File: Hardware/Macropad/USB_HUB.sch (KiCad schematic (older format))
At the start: 25 parts, among them J4 USB_C_Receptacle_USB2.0, J5 USB_C_Receptacle_USB2.0, J6 USB_C_Receptacle_USB2.0, U3 TPS2044D, U4 TUSB2046b, U6 SRV05-4, U7 SRV05-4, U8 SRV05-4, X2 625L3C006M00000

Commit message: First pass of the layout done
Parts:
- removed R12: OPT, resistor_smd:R_0603_1608Metric, symbol Device:R
- removed R30: 4K7, resistor_smd:R_0603_1608Metric, symbol Device:R
- removed U3: TPS2044D, Package_SO:SOIC-16_3.9x9.9mm_P1.27mm, symbol Power_Management:TPS2044D
- added C44, C45, C46: 1uF, Capacitor_smd:C_0603_1608Metric, symbol Device:C
- added R1: 4K7, resistor_smd:R_0603_1608Metric, symbol Device:R
- C37, C39: value 100uF -> 1uF; footprint Capacitor_smd:C_1210_3225Metric -> Capacitor_smd:C_0603_1608Metric
- C38: value 100uF -> 100nF; footprint Capacitor_smd:C_1210_3225Metric -> Capacitor_smd:C_0603_1608Metric
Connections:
- net DM1_N is gone; now on net USB_D1-: R23.1
- net VBUS3 is gone; now on net +5V: C39.1, J6.A4 (VBUS), J6.A9 (VBUS), J6.B4 (VBUS), J6.B9 (VBUS), U8.5 (VP)
- net nOVRCUR1 is gone; now on net +3V3: U4.10 (OVRCUR1)
- net nOVRCUR2 is gone; now on net +3V3: U4.14 (OVRCUR2)
- net nOVRCUR3 is gone; now on net +3V3: U4.18 (OVRCUR3)
- net nOVRCUR4 is gone; now on net +3V3: U4.22 (OVRCUR4)
- net +3V3: now also C37.1, C38.1, X2.1 (EN), R1.2
- net +5V: now also J4.A4 (VBUS), J4.A9 (VBUS), J4.B4 (VBUS), J4.B9 (VBUS), J5.A4 (VBUS), J5.A9 (VBUS), J5.B4 (VBUS), J5.B9 (VBUS), U6.5 (VP), U7.5 (VP), C45.1, C46.1
- net GND: now also C44.1, C45.2, C46.2
- net USB_D2-: now reaches U7.4 (IO3)
- net USB_D2-: now also J5.A7 (D-), J5.B7 (D-), R25.1
- net USB_D3-: now reaches U8.4 (IO3)
- net USB_D3-: now also J6.A7 (D-), J6.B7 (D-), R27.1
- net at U4.4 (RESET): now also C44.2, R1.1
- net USB_D1-: now reaches U6.4 (IO3)
- net USB_D1-: now also J4.A7 (D-), J4.B7 (D-)
- net DM1n renamed D1-
- net D1-: no longer R25.2, U4.15 (DM2)
- removed net DM2_N: J4.A7 (D-), J4.B7 (D-), R25.1, U6.3 (IO2)
- removed net DM3_N: J5.A7 (D-), J5.B7 (D-), R27.1, U7.3 (IO2)
- net DM3n renamed D3-
- removed net DM4_N: J6.A7 (D-), J6.B7 (D-), R29.1, U8.3 (IO2)
- net DM4n renamed D4-
- net DP1_P renamed USB_D1+
- net USB_D1+: now also J4.A6 (D+), J4.B6 (D+), U6.3 (IO2)
- net DP1p renamed D1+
- removed net DP2_P: J4.A6 (D+), J4.B6 (D+), R24.1, U6.1 (IO1)
- net DP2p renamed D2+
- net DP3_P renamed USB_D2+
- net USB_D2+: now also R24.1, U7.3 (IO2); no longer R26.1, U7.1 (IO1)
- net DP3n renamed D3+
- net DP4_P renamed USB_D3+
- net USB_D3+: now also R26.1, U8.3 (IO2); no longer R28.1, U8.1 (IO1)
- net DP4p renamed D4+
- net USBD_N renamed USB_D0-
- net USBD_P renamed USB_D0+
- removed net VBUS1: C37.1, J4.A4 (VBUS), J4.A9 (VBUS), J4.B4 (VBUS), J4.B9 (VBUS), U6.5 (VP)
- removed net VBUS2: C38.1, J5.A4 (VBUS), J5.A9 (VBUS), J5.B4 (VBUS), J5.B9 (VBUS), U7.5 (VP)
- net nPWRON1: no longer names the net of U4.9 (PWRON1)
- net nPWRON2: no longer names the net of U4.13 (PWRON2)
- net nPWRON3: no longer names the net of U4.17 (PWRON3)
- net nPWRON4: no longer names the net of U4.21 (PWRON4)
- new net D2-: R25.2, U4.15 (DM2)
- new net USB_D4+: R28.1
- new net USB_D4-: R29.1
- no-connect marks 9 -> 19
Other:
- note added: "RC rise time 6.5ms aprox"
- note removed: "Downstream power switching"
- note removed: "TODO: \nRC POR circuit\nChoose a 6MHz crystal"
- moved on the sheet: U6, U7, U8

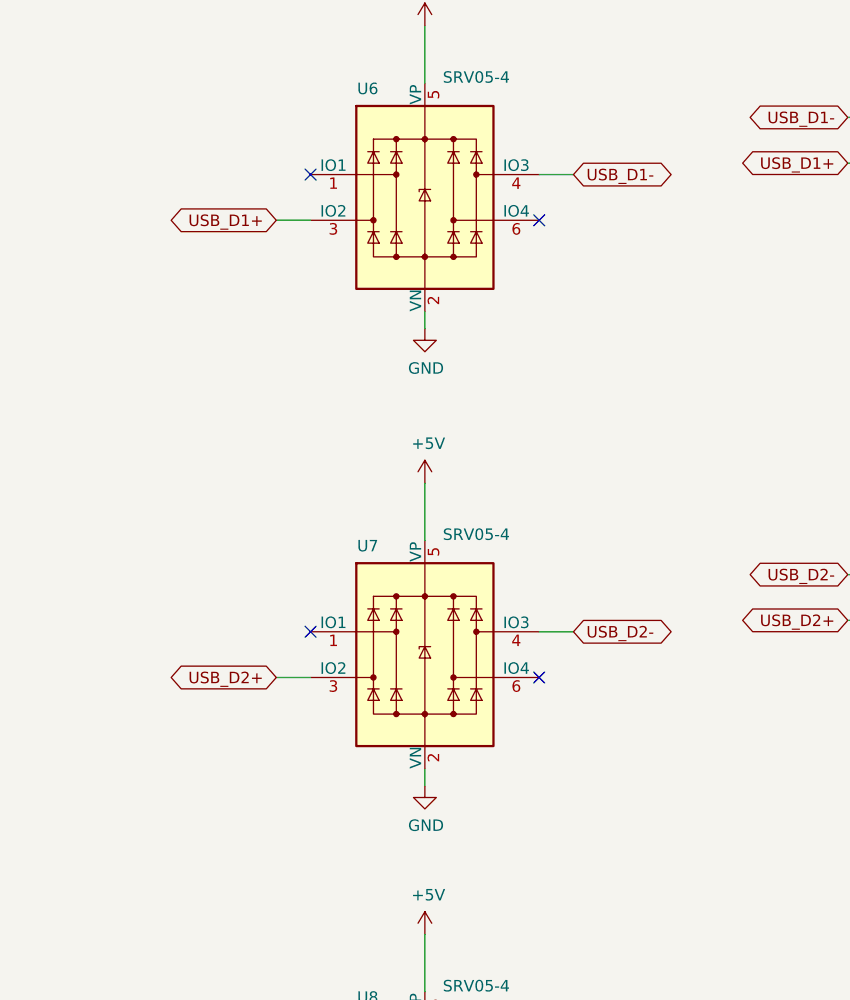
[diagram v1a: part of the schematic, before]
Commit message: Redoing layout with key switches upside down for better LED placement
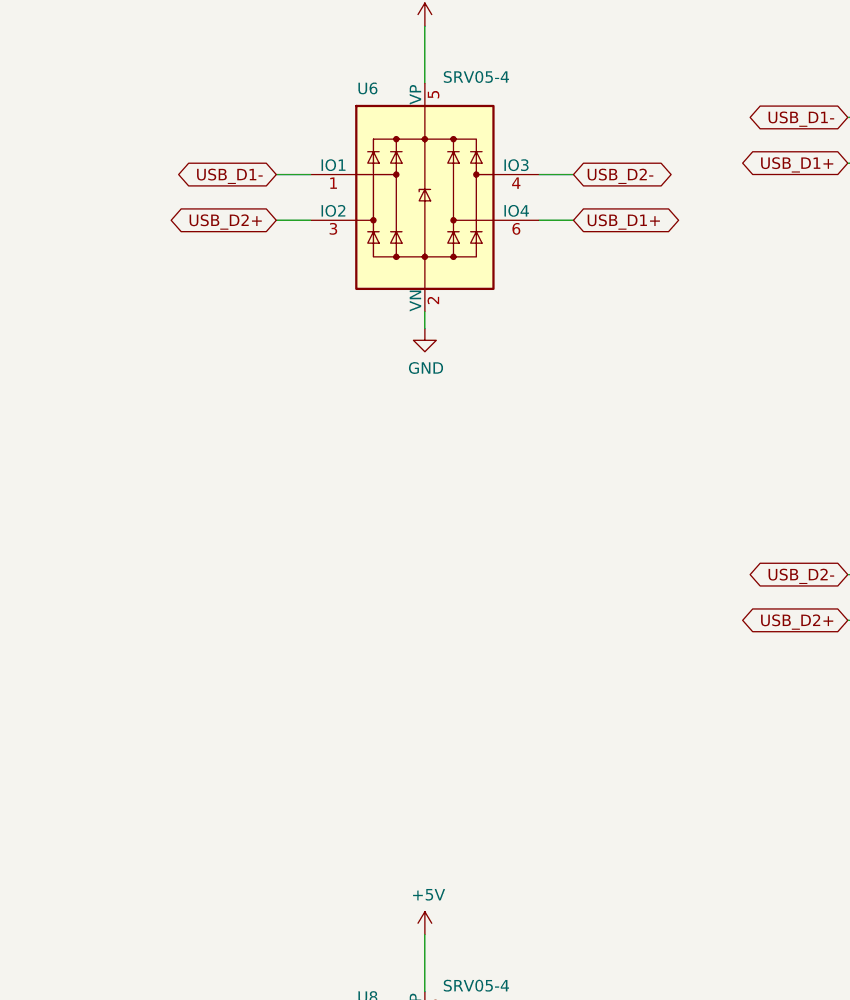
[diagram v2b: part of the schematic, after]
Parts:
- removed U7: SRV05-4, Package_TO_SOT_SMD:SOT-23-6, symbol Power_Protection:SRV05-4
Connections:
- net USB_D1+: now also U6.6 (IO4); no longer U6.3 (IO2)
- net USB_D1-: now also U6.1 (IO1); no longer U6.4 (IO3)
- net USB_D2+: now also U6.3 (IO2)
- net USB_D2-: now also U6.4 (IO3)
- no-connect marks 19 -> 15
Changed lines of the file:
@@
 Connection ~ 9675 5550
-$Comp
-L Power_Protection:SRV05-4 U?
-U 1 1 61242165
-P 7300 3700
-AR Path="/6114D32E/61242165" Ref="U?"  Part="1"
-AR Path="/6247A5CE/61242165" Ref="U7"  Part="1"
-F 0 "U7" H 7050 4175 50  0000 C CNN
-F 1 "SRV05-4" H 7525 4225 50  0000 C CNN
-F 2 "Package_TO_SOT_SMD:SOT-23-6" H 8000 3250 50  0001 C CNN
-F 3 "http://www.onsemi.com/pub/Collateral/SRV05-4-D.PDF" H 7300 3700 50  0001 C CNN
-	1    7300 3700
-	1    0    0    -1
-$EndComp
 $Comp
 L power:GND #PWR?
@@
 $Comp
 L power:GND #PWR?
-U 1 1 6124D41E
-P 7300 4275
-AR Path="/6114D32E/6124D41E" Ref="#PWR?"  Part="1"
-AR Path="/6247A5CE/6124D41E" Ref="#PWR0198"  Part="1"
-F 0 "#PWR0198" H 7300 4025 50  0001 C CNN
-F 1 "GND" H 7305 4102 50  0000 C CNN
-F 2 "" H 7300 4275 50  0001 C CNN
-F 3 "" H 7300 4275 50  0001 C CNN
-	1    7300 4275
-	1    0    0    -1
-$EndComp
-Wire Wire Line
-	7300 4275 7300 4200
-$Comp
-L power:GND #PWR?
 U 1 1 61250FCD
 P 7300 6250
@@
 	7300 6250 7300 6175
 Wire Wire Line
+	6800 1600 6650 1600
+Wire Wire Line
+	7800 1800 7950 1800
+Wire Wire Line
 	7800 1600 7950 1600
-Wire Wire Line
-	6800 1800 6650 1800
-Wire Wire Line
-	7800 3600 7950 3600
-Wire Wire Line
-	6800 3800 6650 3800
 Wire Wire Line
 	7800 5575 7950 5575
@@
 Text GLabel 9150 5350 0    50   BiDi ~ 0
 USB_D3-
-Text GLabel 6650 1800 0    50   BiDi ~ 0
+Text GLabel 7950 1800 2    50   BiDi ~ 0
 USB_D1+
+Text GLabel 6650 1600 0    50   BiDi ~ 0
+USB_D1-
 Text GLabel 7950 1600 2    50   BiDi ~ 0
-USB_D1-
-Text GLabel 6650 3800 0    50   BiDi ~ 0
-USB_D2+
-Text GLabel 7950 3600 2    50   BiDi ~ 0
 USB_D2-
 Text GLabel 6650 5775 0    50   BiDi ~ 0
@@
 NoConn ~ 7800 5775
 NoConn ~ 6800 5575
-NoConn ~ 7800 3800
-NoConn ~ 6800 3600
-NoConn ~ 6800 1600
-NoConn ~ 7800 1800
 Wire Wire Line
 	3850 4425 4025 4425
@@
 $Comp
 L power:+5V #PWR?
-U 1 1 61FE5DA5
-P 7300 2950
-AR Path="/61FE5DA5" Ref="#PWR?"  Part="1"
-AR Path="/60D44BDB/61FE5DA5" Ref="#PWR?"  Part="1"
-AR Path="/60D99CF5/61FE5DA5" Ref="#PWR?"  Part="1"
-AR Path="/6114D32E/61FE5DA5" Ref="#PWR?"  Part="1"
-AR Path="/6247A5CE/61FE5DA5" Ref="#PWR023"  Part="1"
-F 0 "#PWR023" H 7300 2800 50  0001 C CNN
-F 1 "+5V" H 7315 3123 50  0000 C CNN
-F 2 "" H 7300 2950 50  0001 C CNN
-F 3 "" H 7300 2950 50  0001 C CNN
-	1    7300 2950
-	1    0    0    -1
-$EndComp
-$Comp
-L power:+5V #PWR?
 U 1 1 61FEA2EC
 P 7300 4925
@@
 Wire Wire Line
 	7300 4925 7300 5175
-Wire Wire Line
-	7300 2950 7300 3200
 Wire Wire Line
 	7300 950  7300 1200
@@
 	0    1    1    0
 $EndComp
+Wire Wire Line
+	6800 1800 6650 1800
+Text GLabel 6650 1800 0    50   BiDi ~ 0
+USB_D2+
 $EndSCHEMATC

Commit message: Layout done, cleaned up schematic and generated gerbers
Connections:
- no-connect marks 15 -> 21
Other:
- note added: "ESD protection"
- note added: "USB downstream"
- moved on the sheet: C37, C38, C39, C44, C45, C46, J4, J5, J6, R1, R10, R11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
